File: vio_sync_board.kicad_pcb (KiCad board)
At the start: 2 copper layers, 45 x 56 mm, 8 parts, among them J1 Conn_IMU_Pi_Cam, Q1 BSS138, U1 MCP1700x-180xxTT

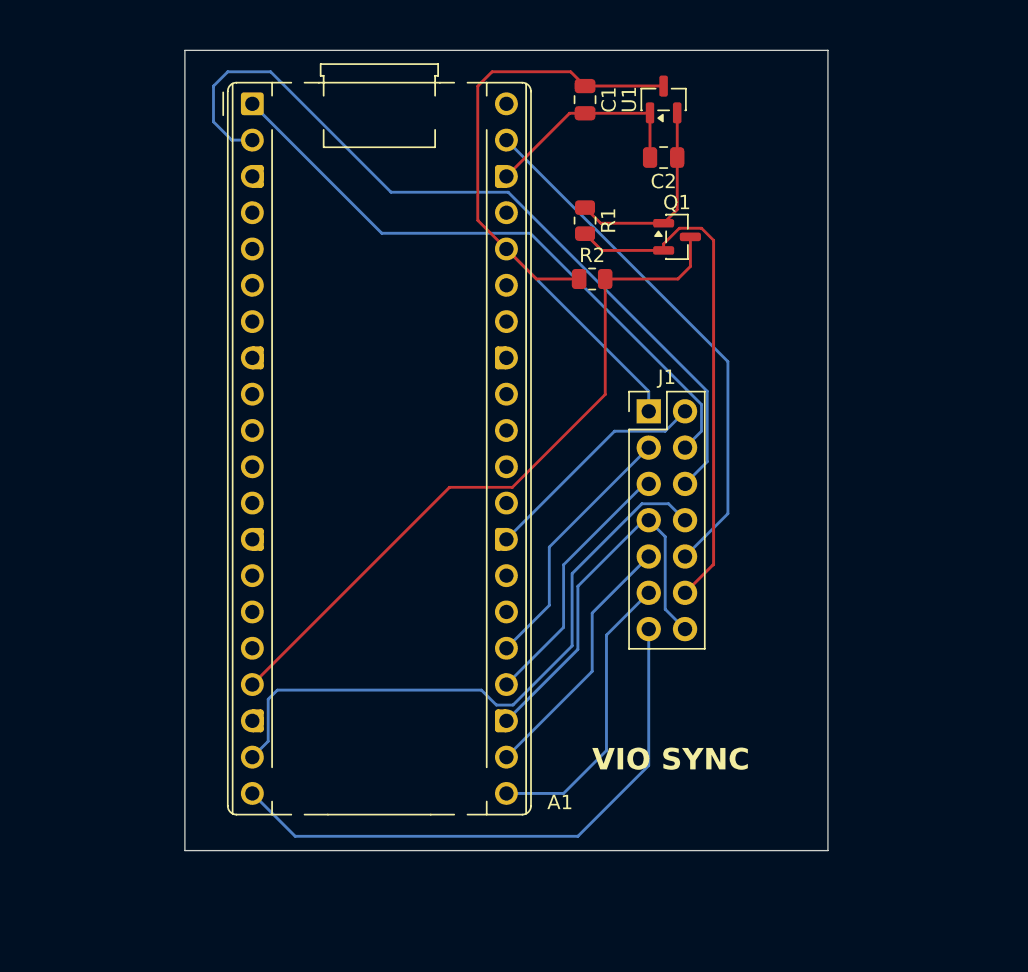
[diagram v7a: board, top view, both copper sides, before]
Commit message: add mounting hole
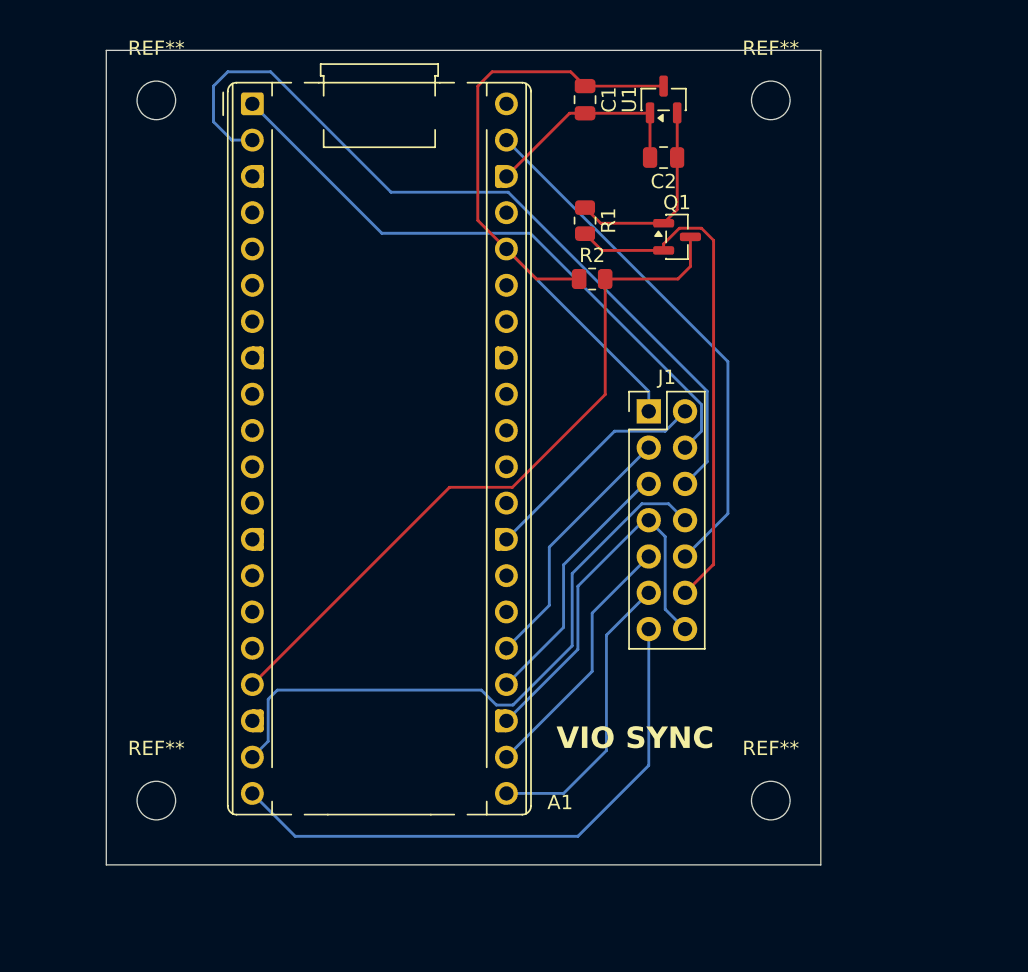
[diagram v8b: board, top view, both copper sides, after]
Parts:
- added REF**: MountingHole_2.7mm_M2.5, MountingHole:MountingHole_2.7mm_M2.5, F.Cu at (44.0, 99.0)
- added REF**: MountingHole_2.7mm_M2.5, MountingHole:MountingHole_2.7mm_M2.5, F.Cu at (44.0, 50.0)
- added REF**: MountingHole_2.7mm_M2.5, MountingHole:MountingHole_2.7mm_M2.5, F.Cu at (87.0, 99.0)
- added REF**: MountingHole_2.7mm_M2.5, MountingHole:MountingHole_2.7mm_M2.5, F.Cu at (87.0, 50.0)
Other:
- board size 45 x 56 mm -> 50 x 57 mm
